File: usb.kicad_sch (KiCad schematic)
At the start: 23 parts, among them J3 USB_C_Receptacle_PowerOnly_6P, J4 Conn_01x02, Q2 AO3401A, SW11 SW_Slide_DPDT, U3 TP4056-42-ESOP8, U4 TPS62170DSG

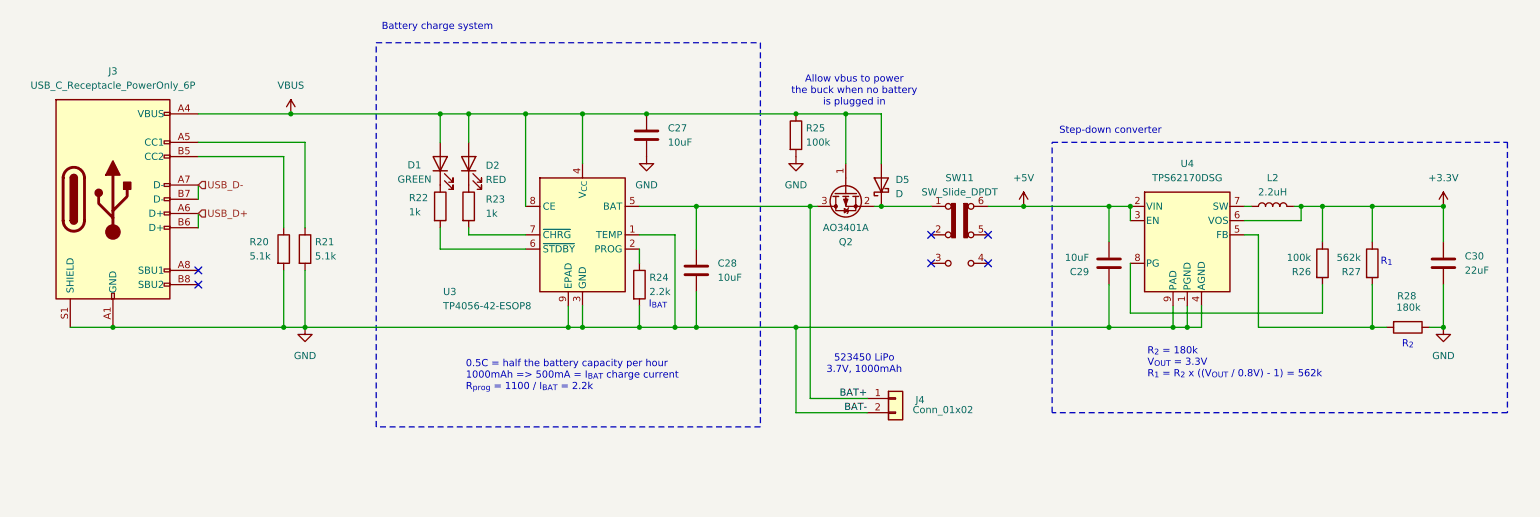
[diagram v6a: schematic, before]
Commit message: check with hardware manual, add comments, add mpns
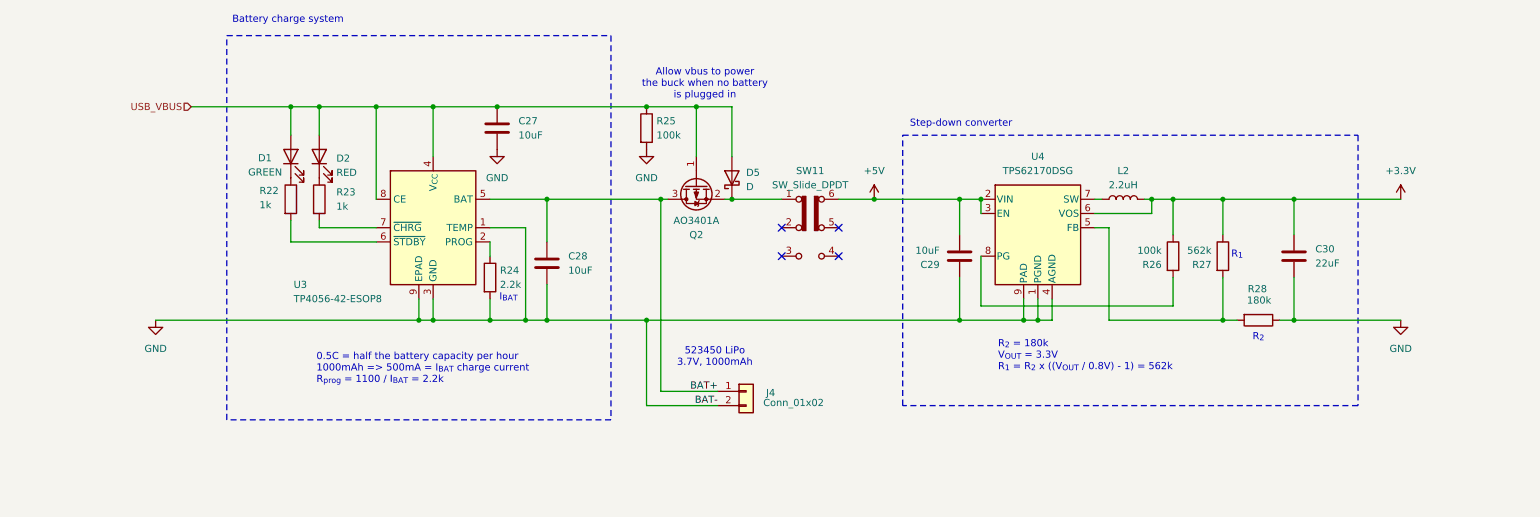
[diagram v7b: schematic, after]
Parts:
- removed J3: USB_C_Receptacle_PowerOnly_6P, Connector_USB:USB_C_Receptacle_GCT_USB4105-xx-A_16P_TopMnt_Horizontal, symbol Connector:USB_C_Receptacle_USB2.0_16P
- removed R20, R21: 5.1k, Resistor_SMD:R_0603_1608Metric, symbol Device:R
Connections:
- net VBUS renamed USB_VBUS
- no-connect marks 6 -> 4
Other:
- moved on the sheet: C27, C28, C29, C30, D1, D2, D5, J4, L2, Q2, R22, R23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

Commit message: fix usb and add esd diodes, some other checks
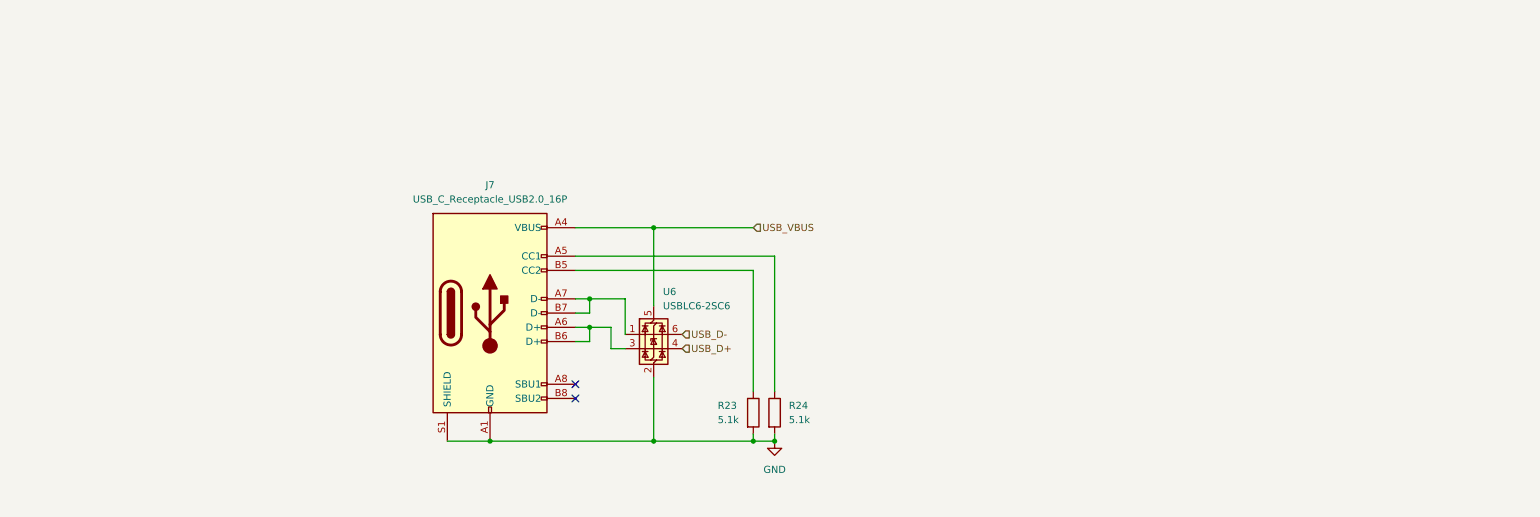
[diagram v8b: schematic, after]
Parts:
- removed C27, C28, C29: 10uF, Capacitor_SMD:C_0603_1608Metric, symbol Device:C
- removed C30: 22uF, Capacitor_SMD:C_0603_1608Metric, symbol Device:C
- removed D1: GREEN, LED_SMD:LED_0603_1608Metric, symbol Device:LED
- removed D2: RED, LED_SMD:LED_0603_1608Metric, symbol Device:LED
- removed D5: D, Diode_SMD:D_SMA, symbol Device:D_Schottky
- removed J4: Conn_01x02, Connector_JST:JST_PH_B2B-PH-K_1x02_P2.00mm_Vertical, symbol Connector_Generic:Conn_01x02
- removed L2: 2.2uH, Inductor_SMD:L_KOHERelec_MDA7030, symbol Device:L
- removed Q2: AO3401A, Package_TO_SOT_SMD:SOT-23, symbol Transistor_FET:AO3401A
- removed R22: 1k, Resistor_SMD:R_0603_1608Metric, symbol Device:R
- removed R25, R26: 100k, Resistor_SMD:R_0603_1608Metric, symbol Device:R
- removed R27: 562k, Resistor_SMD:R_0603_1608Metric, symbol Device:R
- removed R28: 180k, Resistor_SMD:R_0603_1608Metric, symbol Device:R
- removed SW11: SW_Slide_DPDT, Button_Switch_SMD:SW_DPDT_CK_JS202011JCQN, symbol Switch:SW_Slide_DPDT
- removed U3: TP4056-42-ESOP8, Package_SO:SOIC-8-1EP_3.9x4.9mm_P1.27mm_EP2.41x3.3mm_ThermalVias, symbol Battery_Management:TP4056-42-ESOP8
- removed U4: TPS62170DSG, Package_SON:WSON-8-1EP_2x2mm_P0.5mm_EP0.9x1.6mm_ThermalVias, symbol Regulator_Switching:TPS62170DSG
- added J7: USB_C_Receptacle_USB2.0_16P, Connector_USB:USB_C_Receptacle_GCT_USB4105-xx-A_16P_TopMnt_Horizontal, symbol Connector:USB_C_Receptacle_USB2.0_16P
- added U6: USBLC6-2SC6, Package_TO_SOT_SMD:SOT-23-6, symbol Power_Protection:USBLC6-2SC6
- R23: value 1k -> 5.1k
- R24: value 2.2k -> 5.1k
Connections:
- net GND: now also R23.2, J7.A1 (GND), J7.A12 (GND), J7.B1 (GND), J7.B12 (GND), J7.S1 (SHIELD), U6.2 (GND)
- net USB_VBUS: now also J7.A4 (VBUS), J7.A9 (VBUS), J7.B4 (VBUS), J7.B9 (VBUS), U6.5 (VBUS)
- net at R23.1: now also J7.B5 (CC2)
- net at R24.1: now also J7.A5 (CC1)
- new net: J7.A7 (D-), J7.B7 (D-), U6.1 (I/O1)
- new net: J7.A6 (D+), J7.B6 (D+), U6.3 (I/O2)
- new net USB_D+: U6.4 (I/O2)
- new net USB_D-: U6.6 (I/O1)
- no-connect marks 4 -> 2
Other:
- note removed: "0.5C = half the battery capacity per hour 1000mAh => 500mA = I_{BAT} charge current R_{prog} = 1100 / I_{BAT} = 2.2k"
- note removed: "523450 LiPo 3.7V, 1000mAh"
- note removed: "Allow vbus to power the buck when no battery is plugged in"
- note removed: "Battery charge system"
- note removed: "I_{BAT}"
- note removed: "R_{1}"
- note removed: "R_{2}"
- note removed: "R_{2} = 180k V_{OUT} = 3.3V R_{1} = R_{2} x ((V_{OUT} / 0.8V) - 1) = 562k"
- note removed: "Step-down converter"
